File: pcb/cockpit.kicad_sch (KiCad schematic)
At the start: 0 parts

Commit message: Added Front and Rear zone sheets made of CAN and MCU design sheets.
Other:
- added sheet CAN A (can_bus.kicad_sch)
- added sheet CAN B (can_bus.kicad_sch)
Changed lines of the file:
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@@
 	(generator_version "10.0")
 	(paper "A4")
+	(sheet
+		(at 134.62 86.36)
+		(size 38.1 26.67)
+		(exclude_from_sim no)
+		(in_bom yes)
+		(on_board yes)
+		(dnp no)
+		(fields_autoplaced yes)
+		(stroke
+			(width 0.1524)
+			(type solid)
+		)
+		(fill
+			(color 0 0 0 0)
+		)
+		(property "Sheetname" "CAN A"
+			(at 134.62 85.6484 0)
+			(show_name no)
+			(do_not_autoplace no)
+			(effects
+				(font
+					(size 1.27 1.27)
+				)
+				(justify left bottom)
+			)
+		)
+		(property "Sheetfile" "can_bus.kicad_sch"
+			(at 134.62 113.6146 0)
+			(show_name no)
+			(do_not_autoplace no)
+			(effects
+				(font
+					(size 1.27 1.27)
+				)
+				(justify left top)
+			)
+		)
+		(pin "CS" input
+			(at 134.62 88.9 180)
+			(effects
+				(font
+					(size 1.27 1.27)
+				)
+				(justify left)
+			)
+		)
+		(pin "SCK" input
+			(at 134.62 91.44 180)
+			(effects
+				(font
+					(size 1.27 1.27)
+				)
+				(justify left)
+			)
+		)
+		(pin "SI" input
+			(at 134.62 93.98 180)
+			(effects
+				(font
+					(size 1.27 1.27)
+				)
+				(justify left)
+			)
+		)
+		(pin "CAN_H" output
+			(at 172.72 88.9 0)
+			(effects
+				(font
+					(size 1.27 1.27)
+				)
+				(justify right)
+			)
+		)
+		(pin "CAN_L" output
+			(at 172.72 91.44 0)
+			(effects
+				(font
+					(size 1.27 1.27)
+				)
+				(justify right)
+			)
+		)
+		(pin "INT" output
+			(at 172.72 93.98 0)
+			(effects
+				(font
+					(size 1.27 1.27)
+				)
+				(justify right)
+			)
+		)
+		(pin "SO" output
+			(at 172.72 96.52 0)
+			(effects
+				(font
+					(size 1.27 1.27)
+				)
+				(justify right)
+			)
+		)
+		(instances
+			(project "front_rear_dual_can"
+				(path "/11f1b6cb-7ca3-4657-a79b-c672c999e35e/5405e341-74c8-4510-ade9-af70f4b85a3e"
+					(page "12")
+				)
+			)
+		)
+	)
+	(sheet
+		(at 91.44 104.14)
+		(size 30.48 27.94)
+		(exclude_from_sim no)
+		(in_bom yes)
+		(on_board yes)
+		(dnp no)
+		(fields_autoplaced yes)
+		(stroke
+			(width 0.1524)
+			(type solid)
+		)
+		(fill
+			(color 0 0 0 0)
+		)
+		(property "Sheetname" "CAN B"
+			(at 91.44 103.4284 0)
+			(show_name no)
+			(do_not_autoplace no)
+			(effects
+				(font
+					(size 1.27 1.27)
+				)
+				(justify left bottom)
+			)
+		)
+		(property "Sheetfile" "can_bus.kicad_sch"
+			(at 91.44 132.6646 0)
+			(show_name no)
+			(do_not_autoplace no)
+			(effects
+				(font
+					(size 1.27 1.27)
+				)
+				(justify left top)
+			)
+		)
+		(pin "CS" input
+			(at 91.44 106.68 180)
+			(effects
+				(font
+					(size 1.27 1.27)
+				)
+				(justify left)
+			)
+		)
+		(pin "SCK" input
+			(at 91.44 109.22 180)
+			(effects
+				(font
+					(size 1.27 1.27)
+				)
+				(justify left)
+			)
+		)
+		(pin "SI" input
+			(at 91.44 111.76 180)
+			(effects
+				(font
+					(size 1.27 1.27)
+				)
+				(justify left)
+			)
+		)
+		(pin "CAN_H" output
+			(at 121.92 106.68 0)
+			(effects
+				(font
+					(size 1.27 1.27)
+				)
+				(justify right)
+			)
+		)
+		(pin "CAN_L" output
+			(at 121.92 109.22 0)
+			(effects
+				(font
+					(size 1.27 1.27)
+				)
+				(justify right)
+			)
+		)
+		(pin "INT" output
+			(at 121.92 111.76 0)
+			(effects
+				(font
+					(size 1.27 1.27)
+				)
+				(justify right)
+			)
+		)
+		(pin "SO" output
+			(at 121.92 114.3 0)
+			(effects
+				(font
+					(size 1.27 1.27)
+				)
+				(justify right)
+			)
+		)
+		(instances
+			(project "front_rear_dual_can"
+				(path "/11f1b6cb-7ca3-4657-a79b-c672c999e35e/5405e341-74c8-4510-ade9-af70f4b85a3e"
+					(page "13")
+				)
+			)
+		)
+	)
 )

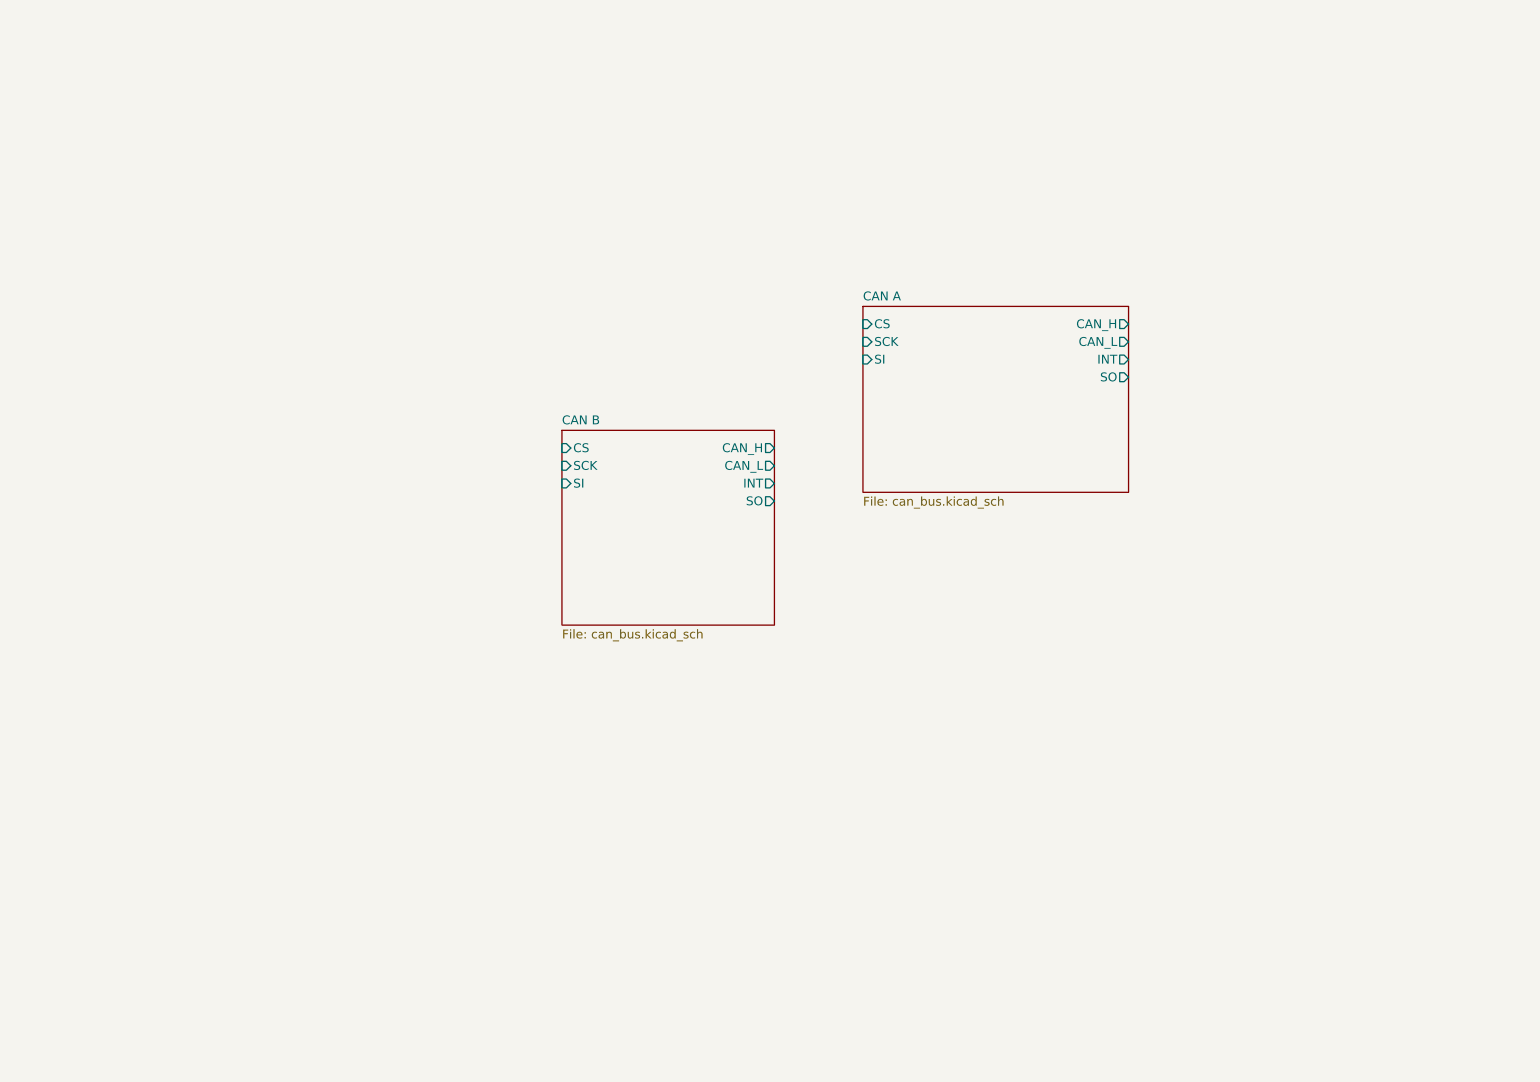
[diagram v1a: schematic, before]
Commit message: Added Cockpit and Power sheets.
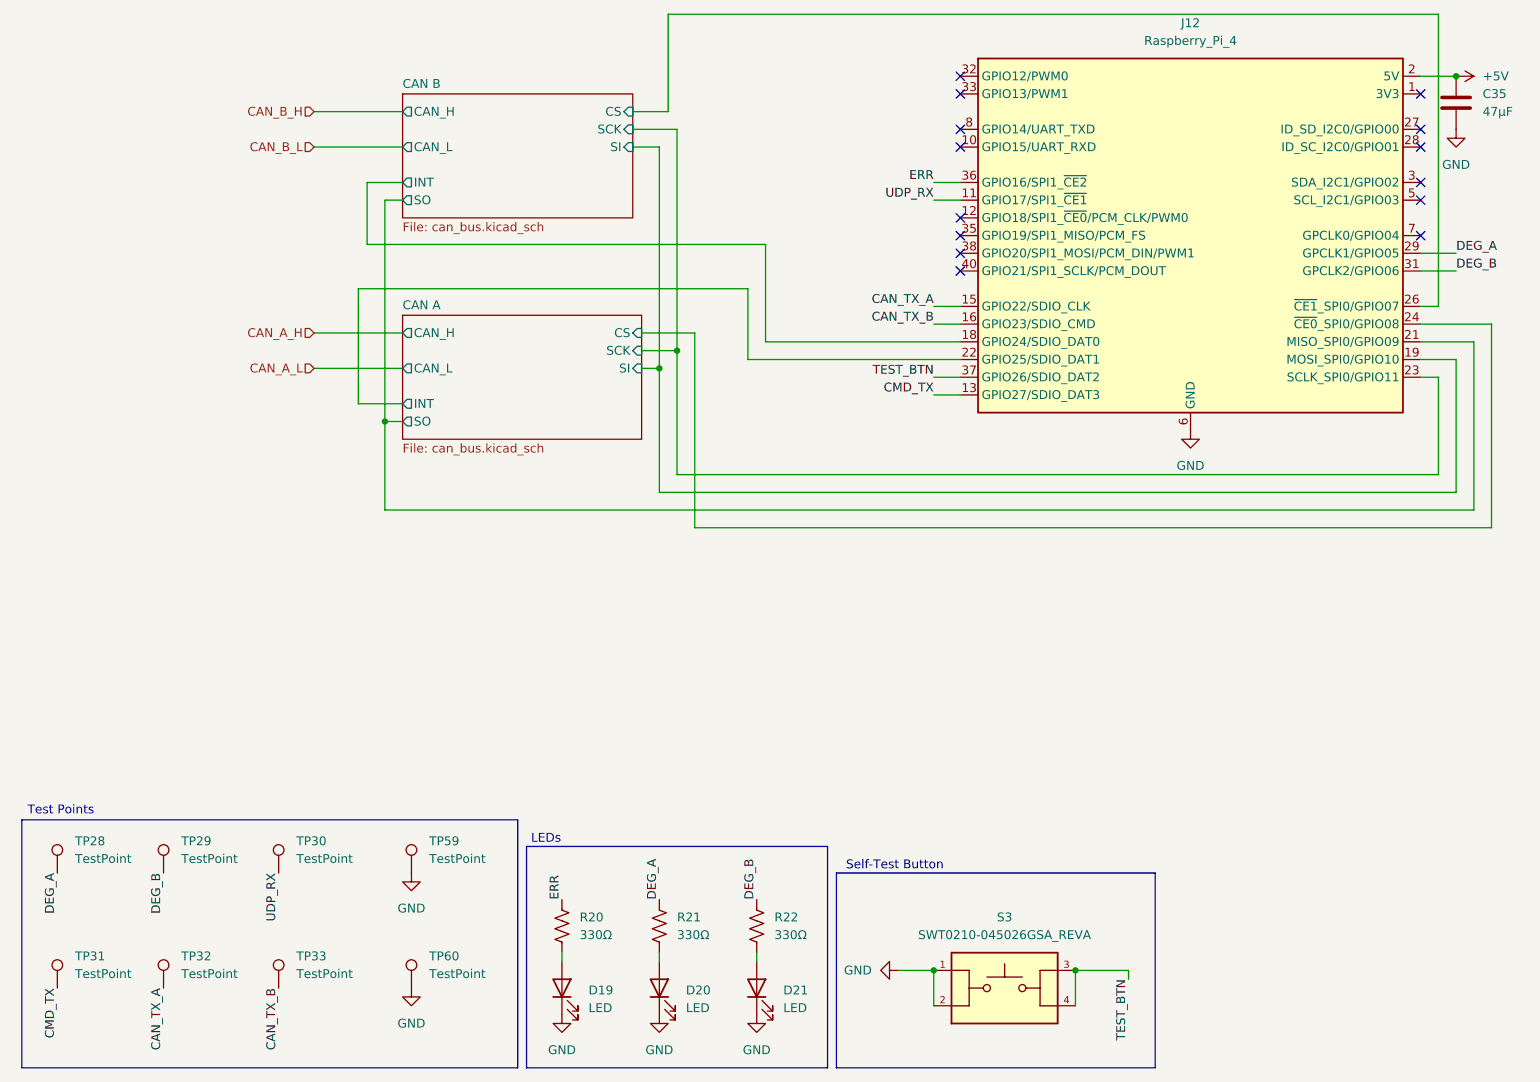
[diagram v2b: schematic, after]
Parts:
- added C35: 47μF, symbol Device:C
- added D19, D20, D21: LED, symbol Device:LED
- added J12: Raspberry_Pi_4, symbol Connector:Raspberry_Pi_4
- added R20, R21, R22: 330Ω, symbol Device:R_US
- added S3: SWT0210-045026GSA_REVA, SWT0210-045026GSA_REVA:SW_SWT0210-045026GSA_REVA, symbol Push Button:SWT0210-045026GSA_REVA
- added TP28, TP29, TP30, TP31, TP32, TP33, TP59, TP60: TestPoint, symbol Connector:TestPoint
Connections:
- net CAN A/CS: now also J12.24 (~{CE0}_SPI0/GPIO08)
- net CAN A/INT: now also J12.22 (GPIO25/SDIO_DAT1)
- net CAN A/SCK: now also J12.23 (SCLK_SPI0/GPIO11)
- net CAN A/SI: now also J12.19 (MOSI_SPI0/GPIO10)
- net CAN A/SO: now also J12.21 (MISO_SPI0/GPIO09)
- net CAN B/CS: now also J12.26 (~{CE1}_SPI0/GPIO07)
- net CAN B/INT: now also J12.18 (GPIO24/SDIO_DAT0)
- new net: J12.1 (3V3), J12.17 (3V3)
- new net: D21.2 (A), R22.2
- new net: D19.2 (A), R20.2
- new net: D20.2 (A), R21.2
- new net +5V: C35.1, J12.2 (5V), J12.4 (5V)
- new net CAN_TX_A: J12.15 (GPIO22/SDIO_CLK), TP32.1
- new net CAN_TX_B: J12.16 (GPIO23/SDIO_CMD), TP33.1
- new net CMD_TX: J12.13 (GPIO27/SDIO_DAT3), TP31.1
- new net DEG_A: J12.29 (GPCLK1/GPIO05), R21.1, TP28.1
- new net DEG_B: J12.31 (GPCLK2/GPIO06), R22.1, TP29.1
- new net ERR: J12.36 (GPIO16/SPI1_~{CE2}), R20.1
- new net GND: C35.2, D19.1 (K), D20.1 (K), D21.1 (K), J12.14 (GND), J12.20 (GND), J12.25 (GND), J12.30 (GND), J12.34 (GND), J12.39 (GND), J12.6 (GND), J12.9 (GND), S3.1, S3.2, TP59.1, TP60.1
- new net TEST_BTN: J12.37 (GPIO26/SDIO_DAT2), S3.3, S3.4
- new net UDP_RX: J12.11 (GPIO17/SPI1_~{CE1}), TP30.1
- no-connect marks 0 -> 14
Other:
- note added: "LEDs"
- note added: "Self-Test Button"
- note added: "Test Points"

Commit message: Added footprints to all components.
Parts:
- C401: renamed from C35; footprint (none) -> Capacitor_SMD:C_1206_3216Metric
- D401: renamed from D19; footprint (none) -> LED_SMD:LED_0603_1608Metric
- D402: renamed from D20; footprint (none) -> LED_SMD:LED_0603_1608Metric
- D403: renamed from D21; footprint (none) -> LED_SMD:LED_0603_1608Metric
- J401: renamed from J12; footprint (none) -> Connector_PinSocket_2.54mm:PinSocket_2x20_P2.54mm_Vertical
- R401: renamed from R20; footprint (none) -> Resistor_SMD:R_0603_1608Metric
- R402: renamed from R21; footprint (none) -> Resistor_SMD:R_0603_1608Metric
- R403: renamed from R22; footprint (none) -> Resistor_SMD:R_0603_1608Metric
- TP401: renamed from TP28; footprint (none) -> TestPoint:TestPoint_Keystone_5015_Micro_Mini
- TP402: renamed from TP31; footprint (none) -> TestPoint:TestPoint_Keystone_5015_Micro_Mini
- TP403: renamed from TP29; footprint (none) -> TestPoint:TestPoint_Keystone_5015_Micro_Mini
- TP404: renamed from TP32; footprint (none) -> TestPoint:TestPoint_Keystone_5015_Micro_Mini
- TP405: renamed from TP30; footprint (none) -> TestPoint:TestPoint_Keystone_5015_Micro_Mini
- TP406: renamed from TP33; footprint (none) -> TestPoint:TestPoint_Keystone_5015_Micro_Mini
- TP407: renamed from TP59; footprint (none) -> TestPoint:TestPoint_Keystone_5015_Micro_Mini
- TP408: renamed from TP60; footprint (none) -> TestPoint:TestPoint_Keystone_5015_Micro_Mini
- renumbered S3 to S401

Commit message: Added CAN Bus connectors and finalized schematic with BOM, LCSC #s, and links to parts.
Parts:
- C401: LCSC (none) -> C96123; MPN (none) -> CL31A476MPHNNNE; Manufacturer (none) -> Samsung
- D401, D402, D403: LCSC (none) -> C94869; MPN (none) -> LTST-C190KRKT; Manufacturer (none) -> Lite-On
- J401: LCSC (none) -> C5124634; MPN (none) -> 2.54-2*20P female
- R401, R402, R403: LCSC (none) -> C105881; MPN (none) -> RC0603FR-07330RL; Manufacturer (none) -> YAGEO
- S401: LCSC (none) -> N/A - shelf part; MPN (none) -> SWT0210-045026GSA; Manufacturer (none) -> GCT
- TP401, TP402, TP403, TP404, TP405, TP406, TP407, TP408: LCSC (none) -> C2906768; MPN (none) -> 5015; Manufacturer (none) -> Keystone Electronics
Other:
- company: (none) -> 18-649 Lab 4: Controller PCB
- title: (none) -> Cockpit Zone: Raspberry Pi 4 Interface

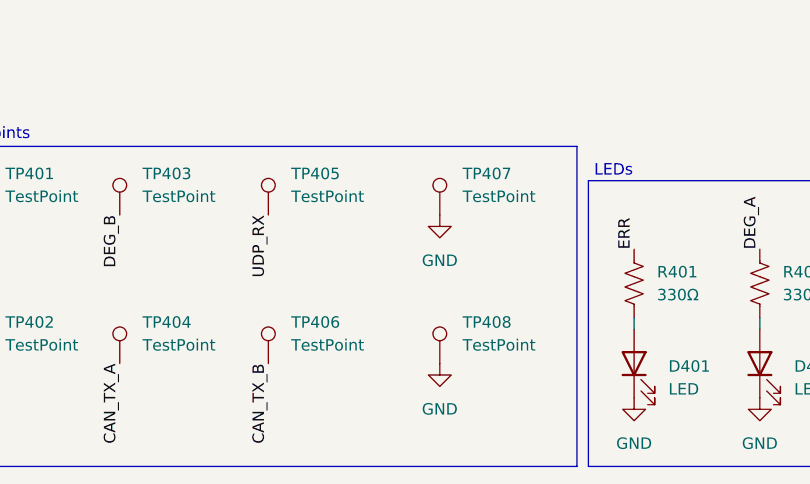
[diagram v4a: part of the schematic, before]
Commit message: Added final touches and test points.
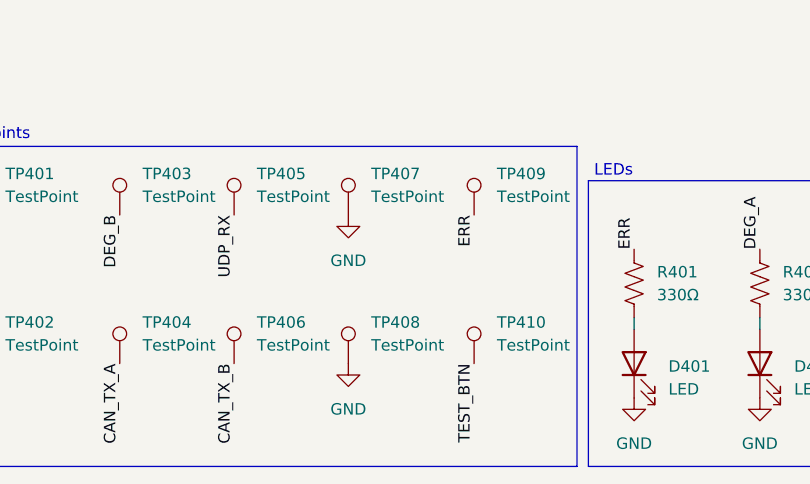
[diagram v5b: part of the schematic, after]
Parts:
- added TP409, TP410: TestPoint, TestPoint:TestPoint_Keystone_5015_Micro_Mini, symbol Connector:TestPoint
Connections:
- net ERR: now also TP409.1
- net TEST_BTN: now also TP410.1
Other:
- moved on the sheet: TP405, TP406, TP407, TP408
